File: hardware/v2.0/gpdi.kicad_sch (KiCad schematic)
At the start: 20 parts, among them J2 GPDI_C_1.3, U1 ECP5U-25F-CABGA256, U6 PCA9306DC1

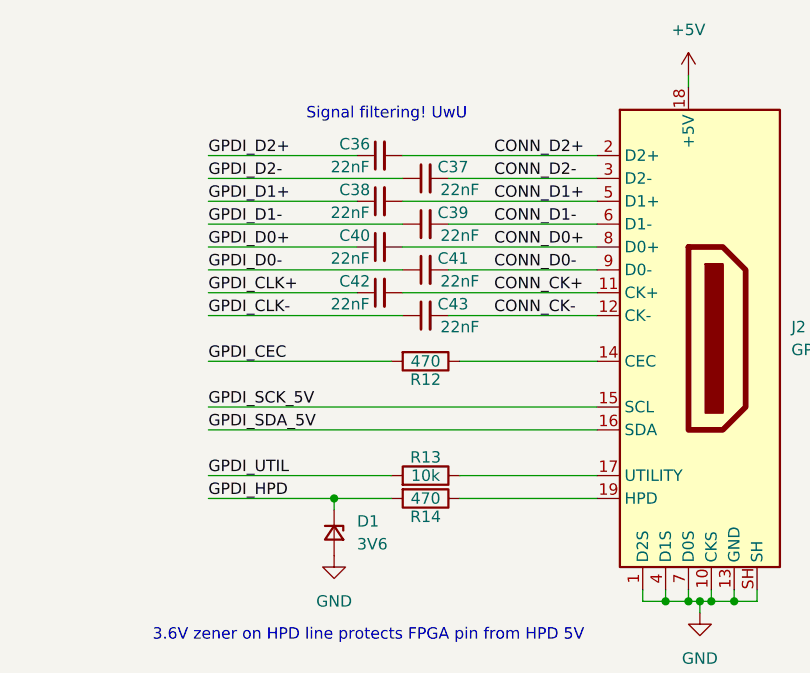
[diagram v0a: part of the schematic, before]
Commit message: BOM fields unification for PCBWay requirements
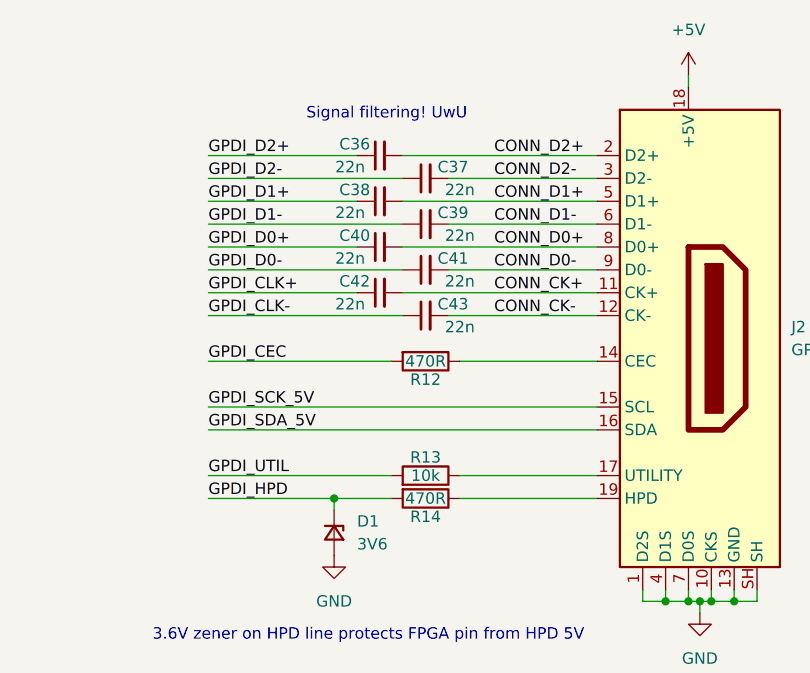
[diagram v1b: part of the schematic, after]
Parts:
- C36, C37, C38, C39, C40, C41, C42, C43: value 22nF -> 22n; MANUFACTURER (none) -> FH; MANUFACTURER_PART_NUMBER (none) -> 0402B223K500NT
- D1: MANUFACTURER (none) -> R+O; MANUFACTURER_PART_NUMBER (none) -> BZT52C3V6S
- J2: MANUFACTURER (none) -> XKB Connection; MANUFACTURER_PART_NUMBER (none) -> A71-05H4-111N1
- R12, R14: value 470 -> 470R; MANUFACTURER (none) -> UNI-ROYAL; MANUFACTURER_PART_NUMBER (none) -> 0402WGF4700TCE
- R13: MANUFACTURER (none) -> UNI-ROYAL; MANUFACTURER_PART_NUMBER (none) -> 0402WGF1002TCE
- R15: MANUFACTURER (none) -> UNI-ROYAL; MANUFACTURER_PART_NUMBER (none) -> 0402WGF1003TCE
- R16, R17: MANUFACTURER (none) -> UNI-ROYAL; MANUFACTURER_PART_NUMBER (none) -> 0402WGF4701TCE
- R18, R19: MANUFACTURER (none) -> UNI-ROYAL; MANUFACTURER_PART_NUMBER (none) -> 0402WGF3301TCE
- U1: MANUFACTURER (none) -> Lattice; MANUFACTURER_PART_NUMBER (none) -> LFE5U-25F-6BG256C
- U6: MANUFACTURER (none) -> NXP; MANUFACTURER_PART_NUMBER (none) -> PCA9306DC1

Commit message: ADC driver power pins bypass
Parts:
- U6: footprint VSSOP-8_2.3x2mm_P0.5mm-exp-mask:VSSOP-8_2.3x2mm_P0.5mm -> Package_SO:VSSOP-8_2.3x2mm_P0.5mm
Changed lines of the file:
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@@
 			)
 		)
-		(property "Footprint" "VSSOP-8_2.3x2mm_P0.5mm-exp-mask:VSSOP-8_2.3x2mm_P0.5mm"
+		(property "Footprint" "Package_SO:VSSOP-8_2.3x2mm_P0.5mm"
 			(at 90.17 153.67 0)
 			(effects

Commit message: Repo links update
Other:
- title: Icepi Zero -> GammaPi Zero
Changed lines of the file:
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@@
 	(paper "A4")
 	(title_block
-		(title "Icepi Zero")
-		(date "2026-01-17")
-		(rev "v2.1")
+		(title "GammaPi Zero")
+		(date "2026-01-25")
+		(rev "v2.3.2")
 		(company "Vadym Vikulin, Chengyin Yao (cheyao)")
-		(comment 1 "https://github.com/vikulin/icepi-zero")
+		(comment 1 "https://github.com/vikulin/gammapi-zero")
 		(comment 2 "License: Solderpad")
 		(comment 9 "OSHWA FR000026")
